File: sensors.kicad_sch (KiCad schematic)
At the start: 9 parts, among them U3 LSM6DS3TR-C, U4 DRV8837CDSGR, U5 DRV8837CDSGR, U6 DRV8837CDSGR

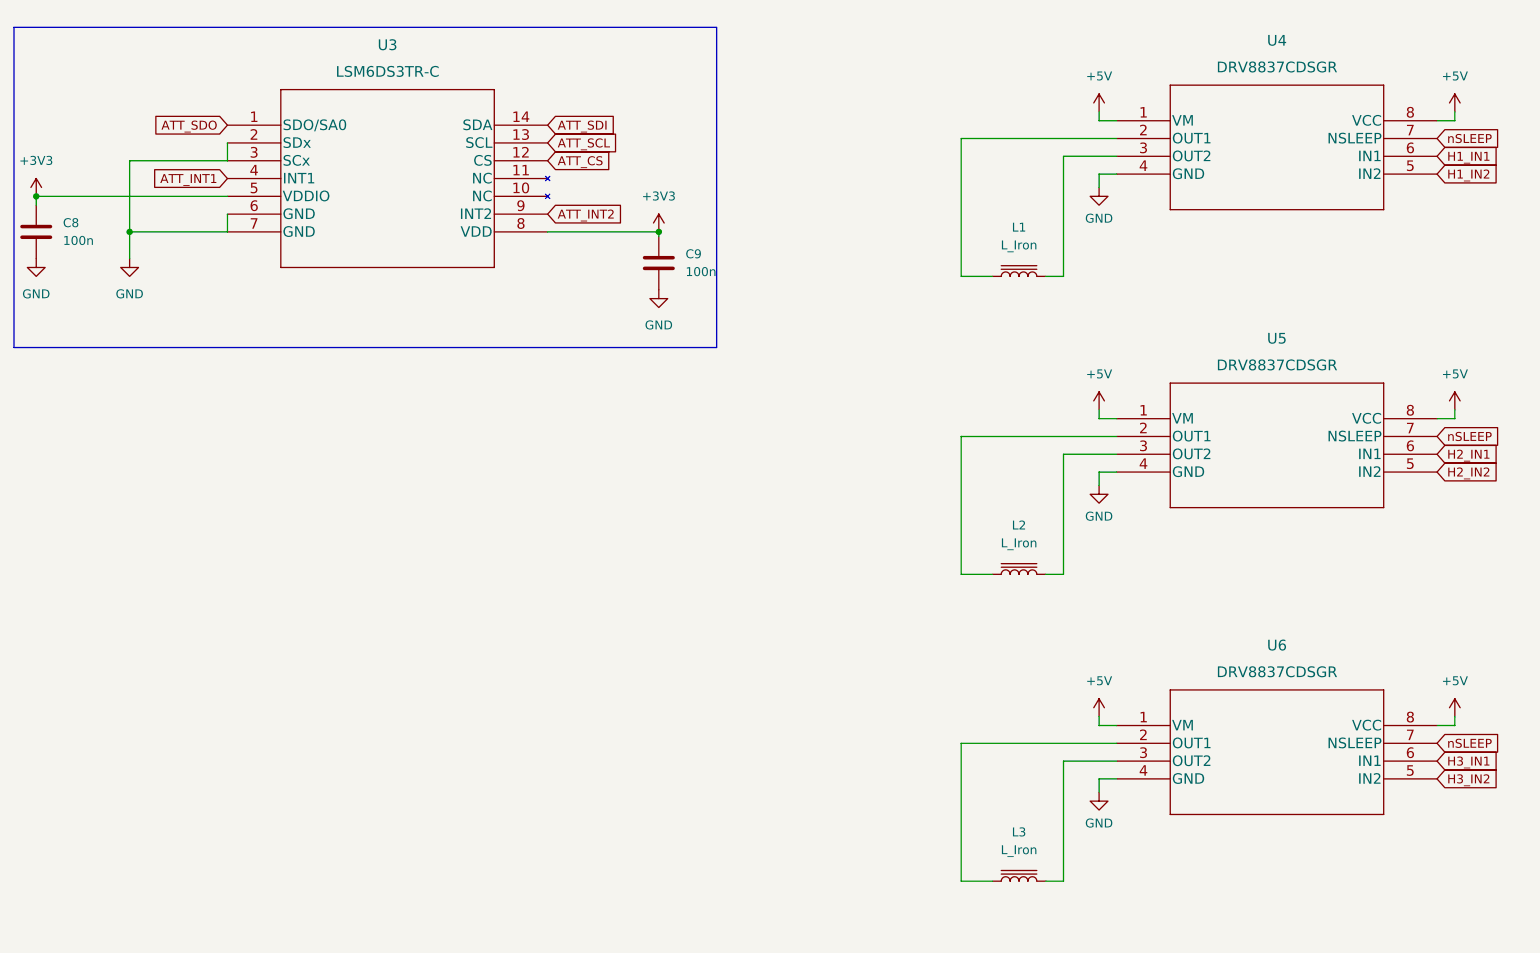
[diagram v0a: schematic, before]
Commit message: added coils
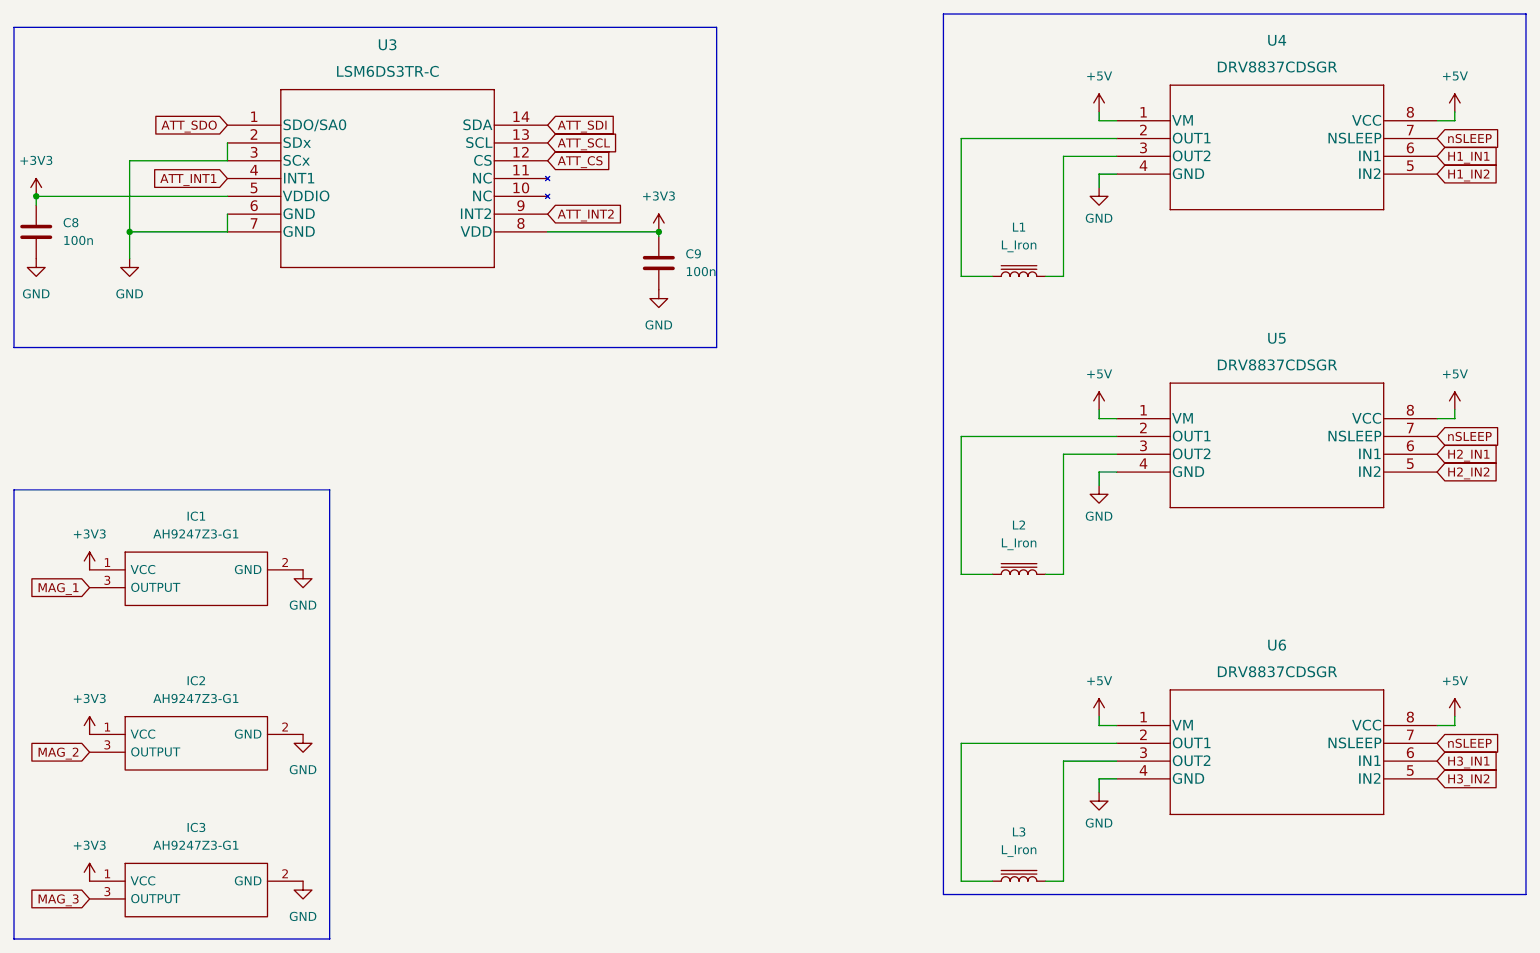
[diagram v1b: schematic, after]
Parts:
- added IC1, IC2, IC3: AH9247Z3-G1, Package_TO_SOT_THT:TO-92Flat, symbol AH9247Z3-G1:AH9247Z3-G1
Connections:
- net +3V3: now also IC1.1 (VCC), IC2.1 (VCC), IC3.1 (VCC)
- net GND: now also IC1.2 (GND), IC2.2 (GND), IC3.2 (GND)
- new net MAG_1: IC1.3 (OUTPUT)
- new net MAG_2: IC2.3 (OUTPUT)
- new net MAG_3: IC3.3 (OUTPUT)

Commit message: new uc
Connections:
- net +5V renamed DRV_VM
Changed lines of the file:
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@@
   (junction (at 48.895 53.34) (diameter 0) (color 0 0 0 0)
   )
+  (junction (at 189.865 123.825) (diameter 0) (color 0 0 0 0)
+  )
+  (junction (at 189.865 37.465) (diameter 0) (color 0 0 0 0)
+  )
   (junction (at 35.56 48.26) (diameter 0) (color 0 0 0 0)
   )
   (junction (at 124.46 53.34) (diameter 0) (color 0 0 0 0)
   )
+  (junction (at 189.865 80.01) (diameter 0) (color 0 0 0 0)
+  )
+  (wire (pts (xy 189.865 80.01) (xy 189.865 74.295))
+    (stroke (width 0) (type default) (color 0 0 0 0))
+  )
   (wire (pts (xy 182.245 146.05) (xy 179.705 146.05))
     (stroke (width 0) (type default) (color 0 0 0 0))
@@
     (stroke (width 0) (type default) (color 0 0 0 0))
   )
-  (wire (pts (xy 238.125 78.74) (xy 238.125 80.01))
-    (stroke (width 0) (type default) (color 0 0 0 0))
-  )
   (wire (pts (xy 35.56 48.26) (xy 35.56 49.53))
     (stroke (width 0) (type default) (color 0 0 0 0))
@@
     (stroke (width 0) (type default) (color 0 0 0 0))
   )
-  (wire (pts (xy 235.585 80.01) (xy 238.125 80.01))
+  (wire (pts (xy 235.585 74.295) (xy 235.585 80.01))
+    (stroke (width 0) (type default) (color 0 0 0 0))
+  )
+  (wire (pts (xy 189.865 74.295) (xy 235.585 74.295))
     (stroke (width 0) (type default) (color 0 0 0 0))
   )
@@
     (stroke (width 0) (type default) (color 0 0 0 0))
   )
-  (wire (pts (xy 187.325 36.195) (xy 187.325 37.465))
+  (wire (pts (xy 235.585 31.75) (xy 235.585 37.465))
     (stroke (width 0) (type default) (color 0 0 0 0))
   )
@@
     (stroke (width 0) (type default) (color 0 0 0 0))
   )
-  (wire (pts (xy 235.585 37.465) (xy 238.125 37.465))
-    (stroke (width 0) (type default) (color 0 0 0 0))
-  )
   (wire (pts (xy 62.865 48.26) (xy 35.56 48.26))
     (stroke (width 0) (type default) (color 0 0 0 0))
@@
     (stroke (width 0) (type default) (color 0 0 0 0))
   )
-  (wire (pts (xy 235.585 123.825) (xy 238.125 123.825))
-    (stroke (width 0) (type default) (color 0 0 0 0))
-  )
   (wire (pts (xy 189.865 85.09) (xy 182.245 85.09))
     (stroke (width 0) (type default) (color 0 0 0 0))
@@
     (stroke (width 0) (type default) (color 0 0 0 0))
   )
+  (wire (pts (xy 235.585 118.11) (xy 235.585 123.825))
+    (stroke (width 0) (type default) (color 0 0 0 0))
+  )
   (wire (pts (xy 62.865 43.18) (xy 48.895 43.18))
     (stroke (width 0) (type default) (color 0 0 0 0))
@@
     (stroke (width 0) (type default) (color 0 0 0 0))
   )
-  (wire (pts (xy 187.325 78.74) (xy 187.325 80.01))
-    (stroke (width 0) (type default) (color 0 0 0 0))
-  )
   (wire (pts (xy 62.865 40.64) (xy 62.865 43.18))
     (stroke (width 0) (type default) (color 0 0 0 0))
@@
     (stroke (width 0) (type default) (color 0 0 0 0))
   )
+  (wire (pts (xy 189.865 118.11) (xy 235.585 118.11))
+    (stroke (width 0) (type default) (color 0 0 0 0))
+  )
+  (wire (pts (xy 189.865 37.465) (xy 189.865 31.75))
+    (stroke (width 0) (type default) (color 0 0 0 0))
+  )
   (wire (pts (xy 187.325 80.01) (xy 189.865 80.01))
     (stroke (width 0) (type default) (color 0 0 0 0))
@@
     (stroke (width 0) (type default) (color 0 0 0 0))
   )
-  (wire (pts (xy 238.125 122.555) (xy 238.125 123.825))
-    (stroke (width 0) (type default) (color 0 0 0 0))
-  )
   (polyline (pts (xy 132.715 69.85) (xy 132.715 24.13))
     (stroke (width 0) (type default) (color 0 0 0 0))
@@
     (stroke (width 0) (type default) (color 0 0 0 0))
   )
+  (wire (pts (xy 189.865 31.75) (xy 235.585 31.75))
+    (stroke (width 0) (type default) (color 0 0 0 0))
+  )
   (wire (pts (xy 189.865 40.005) (xy 167.64 40.005))
     (stroke (width 0) (type default) (color 0 0 0 0))
@@
     (stroke (width 0) (type default) (color 0 0 0 0))
   )
+  (wire (pts (xy 189.865 123.825) (xy 189.865 118.11))
+    (stroke (width 0) (type default) (color 0 0 0 0))
+  )
   (wire (pts (xy 108.585 53.34) (xy 124.46 53.34))
     (stroke (width 0) (type default) (color 0 0 0 0))
@@
     (stroke (width 0) (type default) (color 0 0 0 0))
   )
-  (wire (pts (xy 238.125 36.195) (xy 238.125 37.465))
-    (stroke (width 0) (type default) (color 0 0 0 0))
-  )
   (wire (pts (xy 62.865 50.8) (xy 62.865 53.34))
     (stroke (width 0) (type default) (color 0 0 0 0))
@@
     (stroke (width 0) (type default) (color 0 0 0 0))
   )
-  (wire (pts (xy 187.325 122.555) (xy 187.325 123.825))
-    (stroke (width 0) (type default) (color 0 0 0 0))
-  )
   (polyline (pts (xy 32.385 24.13) (xy 132.715 24.13))
     (stroke (width 0) (type default) (color 0 0 0 0))
@@
     (stroke (width 0) (type default) (color 0 0 0 0))
   )
+  (global_label "DRV_VM" (shape input) (at 187.325 80.01 180) (fields_autoplaced)
+    (effects (font (size 1.27 1.27)) (justify right))
+    (property "Intersheet References" "${INTERSHEET_REFS}" (id 0) (at 177.7757 79.9306 0)
+      (effects (font (size 1.27 1.27)) (justify right) hide)
+    )
+  )
   (global_label "ATT_SDO" (shape input) (at 62.865 38.1 180) (fields_autoplaced)
     (effects (font (size 1.27 1.27)) (justify right))
@@
     )
   )
+  (global_label "DRV_VM" (shape input) (at 187.325 37.465 180) (fields_autoplaced)
+    (effects (font (size 1.27 1.27)) (justify right))
+    (property "Intersheet References" "${INTERSHEET_REFS}" (id 0) (at 177.7757 37.3856 0)
+      (effects (font (size 1.27 1.27)) (justify right) hide)
+    )
+  )
   (global_label "H2_IN1" (shape input) (at 235.585 85.09 0) (fields_autoplaced)
     (effects (font (size 1.27 1.27)) (justify left))
@@
     (property "Intersheet References" "${INTERSHEET_REFS}" (id 0) (at 118.4971 40.5606 0)
       (effects (font (size 1.27 1.27)) (justify left) hide)
+    )
+  )
+  (global_label "DRV_VM" (shape input) (at 187.325 123.825 180) (fields_autoplaced)
+    (effects (font (size 1.27 1.27)) (justify right))
+    (property "Intersheet References" "${INTERSHEET_REFS}" (id 0) (at 177.7757 123.7456 0)
+      (effects (font (size 1.27 1.27)) (justify right) hide)
     )
   )
@@
     )
     (property "Datasheet" "" (id 3) (at 124.46 61.595 0)
-      (effects (font (size 1.27 1.27)) hide)
-    )
-    (pin "1")
-  )
-  (symbol (lib_id "power:+5V") (at 238.125 78.74 0) (unit 1)
-    (in_bom yes) (on_board yes) (fields_autoplaced)
-    (property "Reference" "#PWR015" (id 0) (at 238.125 82.55 0)
-      (effects (font (size 1.27 1.27)) hide)
-    )
-    (property "Value" "+5V" (id 1) (at 238.125 73.66 0))
-    (property "Footprint" "" (id 2) (at 238.125 78.74 0)
-      (effects (font (size 1.27 1.27)) hide)
-    )
-    (property "Datasheet" "" (id 3) (at 238.125 78.74 0)
       (effects (font (size 1.27 1.27)) hide)
     )
@@
     (pin "3")
   )
-  (symbol (lib_id "power:+5V") (at 238.125 122.555 0) (unit 1)
-    (in_bom yes) (on_board yes) (fields_autoplaced)
-    (property "Reference" "#PWR016" (id 0) (at 238.125 126.365 0)
-      (effects (font (size 1.27 1.27)) hide)
-    )
-    (property "Value" "+5V" (id 1) (at 238.125 117.475 0))
-    (property "Footprint" "" (id 2) (at 238.125 122.555 0)
-      (effects (font (size 1.27 1.27)) hide)
-    )
-    (property "Datasheet" "" (id 3) (at 238.125 122.555 0)
-      (effects (font (size 1.27 1.27)) hide)
-    )
-    (pin "1")
-  )
   (symbol (lib_id "power:GND") (at 35.56 57.15 0) (unit 1)
     (in_bom yes) (on_board yes) (fields_autoplaced)
@@
     )
     (property "Datasheet" "" (id 3) (at 35.56 57.15 0)
-      (effects (font (size 1.27 1.27)) hide)
-    )
-    (pin "1")
-  )
-  (symbol (lib_id "power:+5V") (at 238.125 36.195 0) (unit 1)
-    (in_bom yes) (on_board yes) (fields_autoplaced)
-    (property "Reference" "#PWR0111" (id 0) (at 238.125 40.005 0)
-      (effects (font (size 1.27 1.27)) hide)
-    )
-    (property "Value" "+5V" (id 1) (at 238.125 31.115 0))
-    (property "Footprint" "" (id 2) (at 238.125 36.195 0)
-      (effects (font (size 1.27 1.27)) hide)
-    )
-    (property "Datasheet" "" (id 3) (at 238.125 36.195 0)
       (effects (font (size 1.27 1.27)) hide)
     )
@@
     (pin "1")
   )
-  (symbol (lib_id "power:+5V") (at 187.325 78.74 0) (unit 1)
-    (in_bom yes) (on_board yes) (fields_autoplaced)
-    (property "Reference" "#PWR011" (id 0) (at 187.325 82.55 0)
-      (effects (font (size 1.27 1.27)) hide)
-    )
-    (property "Value" "+5V" (id 1) (at 187.325 73.66 0))
-    (property "Footprint" "" (id 2) (at 187.325 78.74 0)
-      (effects (font (size 1.27 1.27)) hide)
-    )
-    (property "Datasheet" "" (id 3) (at 187.325 78.74 0)
-      (effects (font (size 1.27 1.27)) hide)
-    )
-    (pin "1")
-  )
-  (symbol (lib_id "power:+5V") (at 187.325 36.195 0) (unit 1)
-    (in_bom yes) (on_board yes) (fields_autoplaced)
-    (property "Reference" "#PWR0109" (id 0) (at 187.325 40.005 0)
-      (effects (font (size 1.27 1.27)) hide)
-    )
-    (property "Value" "+5V" (id 1) (at 187.325 31.115 0))
-    (property "Footprint" "" (id 2) (at 187.325 36.195 0)
-      (effects (font (size 1.27 1.27)) hide)
-    )
-    (property "Datasheet" "" (id 3) (at 187.325 36.195 0)
-      (effects (font (size 1.27 1.27)) hide)
-    )
-    (pin "1")
-  )
   (symbol (lib_id "power:GND") (at 73.66 101.6 0) (unit 1)
     (in_bom yes) (on_board yes) (fields_autoplaced)
@@
       (effects (font (size 1.27 1.27)) hide)
     )
-    (pin "1")
-  )
-  (symbol (lib_id "power:+5V") (at 187.325 122.555 0) (unit 1)
-    (in_bom yes) (on_board yes) (fields_autoplaced)
-    (property "Reference" "#PWR013" (id 0) (at 187.325 126.365 0)
-      (effects (font (size 1.27 1.27)) hide)
-    )
-    (property "Value" "+5V" (id 1) (at 187.325 117.475 0))
-    (property "Footprint" "" (id 2) (at 187.325 122.555 0)
-      (effects (font (size 1.27 1.27)) hide)
-    )
-    (property "Datasheet" "" (id 3) (at 187.325 122.555 0)
-      (effects (font (size 1.27 1.27)) hide)
-    )
